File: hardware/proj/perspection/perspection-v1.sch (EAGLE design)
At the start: 233 parts, among them J1 MICRO-USB-10118192-0001LF, J2 1X6-PTSA_1.5/6-3.5-Z, J3 1X2-PTSA_1.5/2-3.5-Z, J4 1X2-JST-PH-SMD, J5 1X2-0428202213, J6 JTAG-ARM_TC-10, J7 JTAG-ARM_TC-10, J8 1X3-0.1IN_THRUHOLE, Q1 NMOS-CSD18533Q5A, Q10 NMOS-CSD18533Q5A, Q11 IRFML8244TRPBF, Q2 NMOS-CSD18533Q5A, Q3 NMOS-CSD18533Q5A, Q4 NMOS-CSD18533Q5A, Q5 NMOS-CSD18533Q5A, Q6 NMOS-CSD18533Q5A, Q7 NMOS-CSD18533Q5A, Q8 BSS138L, Q9 BSS138L, U1 ATUM, U10 DRV8301DCAR, U11 OPA2374AIDCNR, U12 OPA170AIDBVR, U13 BNO055, U2 FT232RQ, U3 TPS79933DDCR, U4 MCP73831T-2ACI/OT, U5 TMS320F28069MPZT, U6 DRV8801PWPR, U7 DRV8801PWPR, U8 DRV8801PWPR, U9 DRV8801PWPR, Y1 32.768kHz

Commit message: holy fucking shit 81 airwires to go
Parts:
- added J9: 1X2-PTSA_1.5/2-3.5-Z, perspection:1X2-PTSA_1.5/2-3.5-Z
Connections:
- net N$6 renamed D_P
- net N$7 renamed D_N
- new net N$16: C69.1, U5.1.VDD4
- new net N$17: C68.1, U5.1.VDD3
- new net N$21: C66.1, U5.1.VDD1
- new net N$6: C71.1, U5.1.VDD6
- new net N$7: C70.1, U5.1.VDD5
- net +12V: now also J9.1
- net +12V_GND: now also J9.2
- net N$58: now also U5.1.VDD2; no longer C66.1, C68.1, C69.1, C70.1, C71.1, U5.1.VDD
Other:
- moved on the sheet: C66, C67, C68, C69, C70, C71, C72, C73, C74, C75, C76, C77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

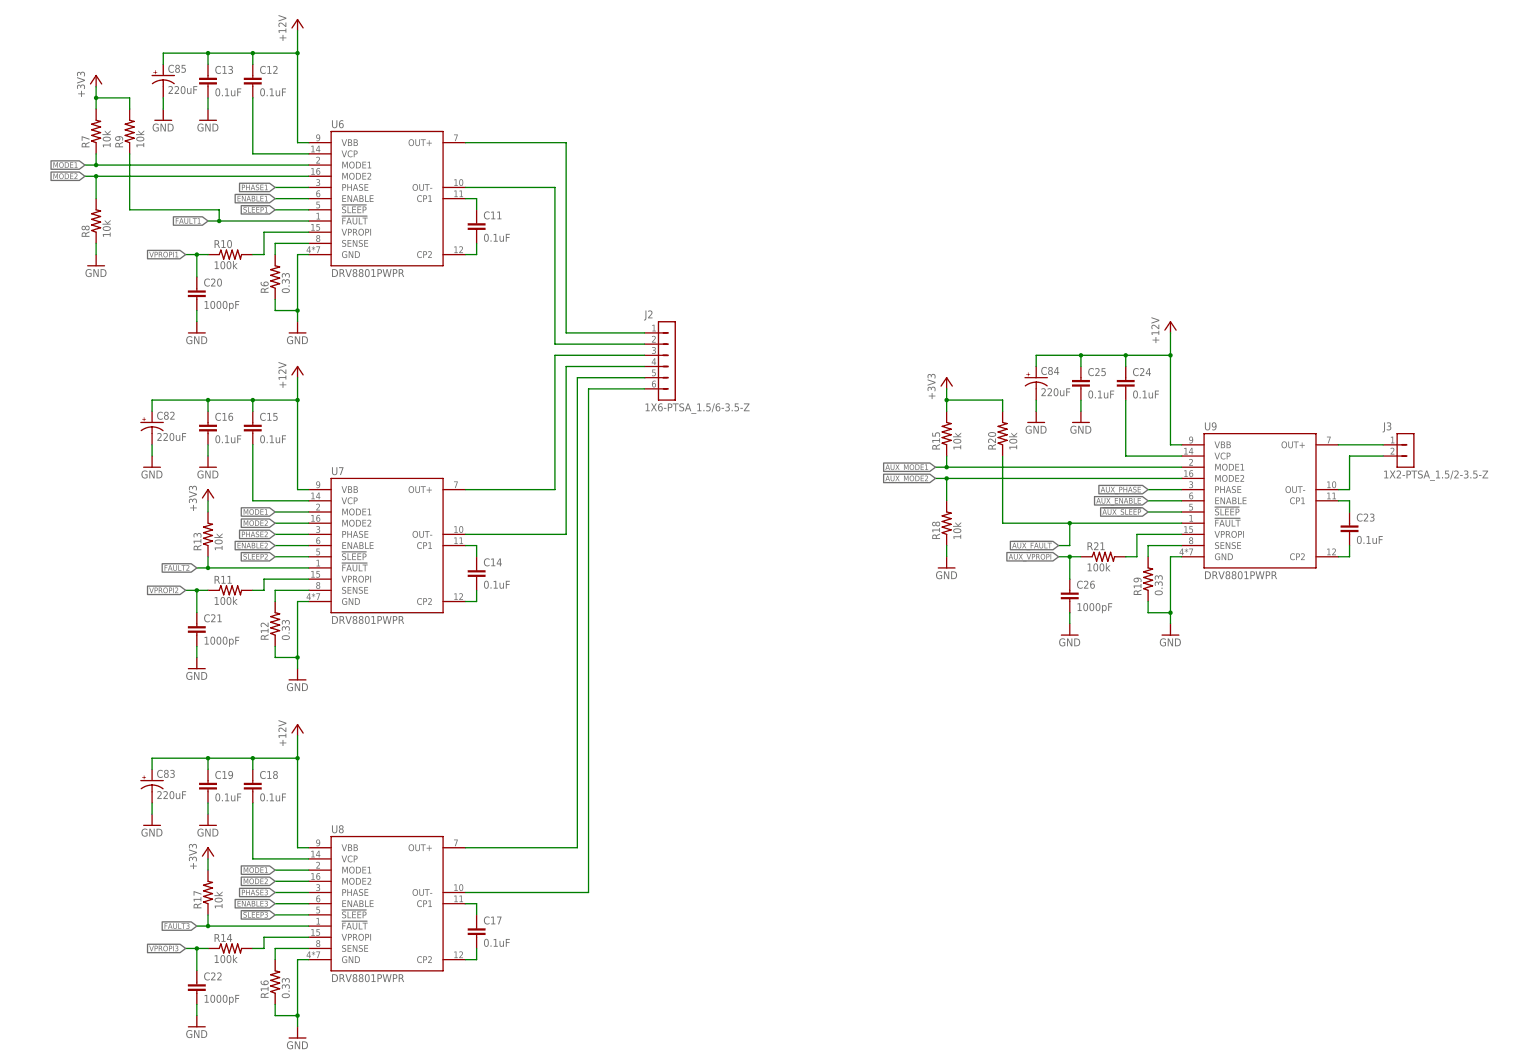
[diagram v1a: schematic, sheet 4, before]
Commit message: 26 airwires!
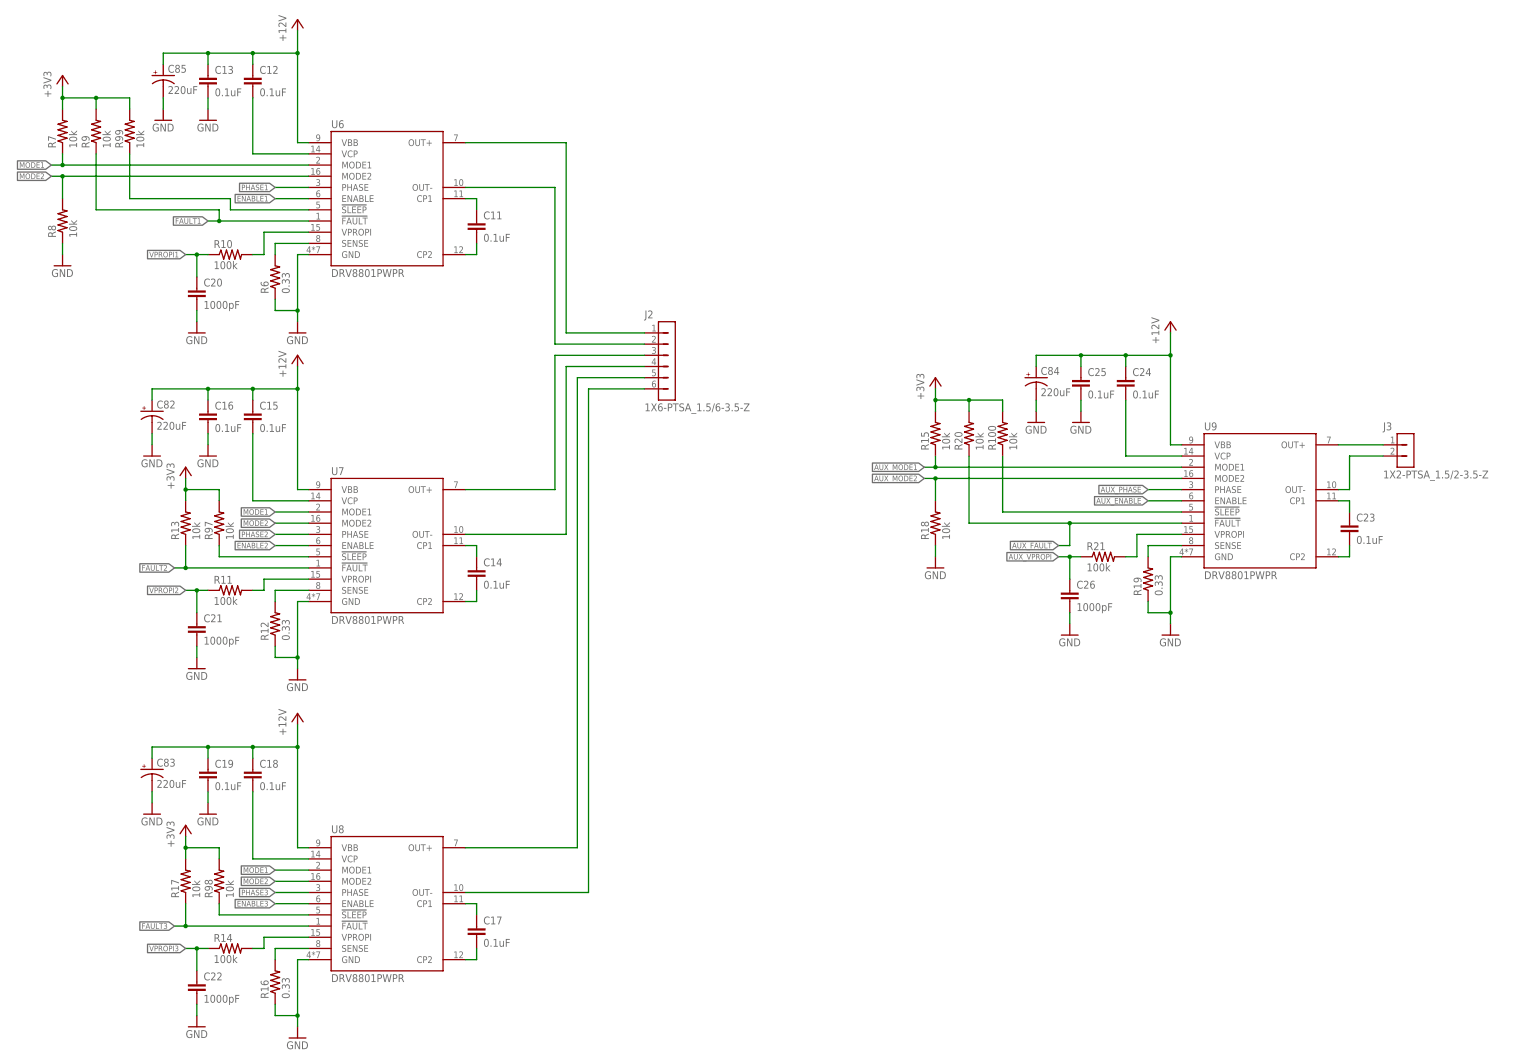
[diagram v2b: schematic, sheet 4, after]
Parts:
- added R100, R97, R98, R99: 10k, perspection:R0402
- added R101, R102, R103, R104, R105, R106, R107, R108, R93, R94, R95, R96: 0, perspection:R0402
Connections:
- net N$16 renamed VDD4
- net N$17 renamed VDD3
- net N$21 renamed VDD1
- net N$58 renamed VDD2
- net N$6 renamed VDD6
- net N$7 renamed VDD5
- removed net ATUM_B3: U1.B3
- removed net ATUM_B4: U1.B4
- new net ATUM_ENCODER_A: R107.1
- new net ATUM_ENCODER_B: R108.1
- new net N$25: R93.1, U5.1.ADC_INB2/COMP1B/AIO10
- new net N$26: R94.1, U5.1.ADC_INB1
- new net N$27: R95.1, U5.1.ADC_INB0
- new net N$31: R96.1, U5.1.ADC_INA6/COMP3A/AIO6
- new net N$32: R102.2, U5.2.GPIO3/EPWM2B/SPISOMIA/COMP2OUT
- new net N$43: R103.2, U5.2.GPIO2/EPWM2A
- new net N$44: R104.2, U5.2.GPIO1/EPWM1B/COMP1OUT
- new net N$46: R101.2, U5.2.GPIO0/EPWM1A
- new net N$47: R105.2, U1.B4
- new net N$48: R106.2, U1.B3
- net !AUX_SLEEP: now also R100.1
- net !SLEEP1: now also R99.1
- net !SLEEP2: now also R97.1
- net !SLEEP3: now also R98.1
- net +3V3: now also R100.2, R97.2, R98.2, R99.2
- net ATUM_C0: now also R108.2
- net ATUM_C1: now also R107.2
- net AUX_ENABLE: now also R101.1, R105.1
- net AUX_PHASE: now also R106.1
- net AUX_VPROPI: now also R96.2
- net ENABLE1: now also R104.1
- net ENABLE2: now also R103.1
- net ENABLE3: now also R102.1
- net VPROPI1: now also R95.2
- net VPROPI2: now also R94.2
- net VPROPI3: now also R93.2
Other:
- moved on the sheet: C15, C16, C18, C19, C82, C83, R13, R15, R17, R18, R20, R40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

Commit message: JASON TAKE THE WHEEL
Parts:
- added C95: 4.7uF, perspection:C0603
- added J10: 1X5, perspection:1X5
- added R109, R111, R113: 23.2k, perspection:R0402
- added R110, R112, R114: 45.2k, perspection:R0402
- added R115, R116, R117, R118: 0, perspection:R0402
- added R119, R120, R121, R122: (no value), perspection:R0402
- added U14: TPS81256, perspection:TPS81256
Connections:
- net N$91 renamed PICCOLO_TMS
- net N$92 renamed PICCOLO_TCK
- net N$93 renamed PICCOLO_TDI
- net N$95 renamed !PICCOLO_TRST
- removed net ATUM_C2: U1.C2
- removed net ATUM_ENCODER_A: R107.1
- removed net ATUM_ENCODER_B: R108.1
- removed net N$94: J7.TDO, U5.1.TDO/GPIO37
- new net !SPI_CS: R117.2, U1.C2
- new net ENC_PWR: C95.1, J10.2, U14.VOUT
- new net EQEP1A: R107.1, R111.1, R112.2, U5.2.GPIO20/EQEP1A/MDXA/COMP1OUT
- new net EQEP1B: R108.1, R109.1, R110.2, U5.2.GPIO21/EQEP1B/MDRA/COMP2OUT
- new net EQEP1I: R113.1, R114.2, U5.2.GPIO23/EQEP1I/MFSXA/SCIRXDB
- new net GPIO_34: R121.1, R122.2, U5.2.GPIO34/COMP2OUT/COMP3OUT
- new net N$16: J10.3, R111.2
- new net N$17: J10.4, R113.2
- new net N$6: J10.1, R109.2
- new net PICCOLO_TDO: J7.TDO, R119.1, R120.2, U5.1.TDO/GPIO37
- new net _!SPI_CS: R117.1, U5.2.GPIO57/!SPISTEA!/EQEP2S/HRCAP4
- new net _SPI_MISO: R116.1, U5.2.GPIO55/SPISOMIA/EQEP2B/HRCAP2
- new net _SPI_MOSI: R115.1, U5.2.GPIO54/SPISIMOA/EQEP2A/HRCAP1
- new net _SPI_SCK: R118.1, U5.2.GPIO56/SPICLKA/EQEP2I/HRCAP3
- net +3V3: now also R119.2, R121.2, U14.EN, U14.VIN
- net GND: now also C95.2, J10.5, R110.1, R112.1, R114.1, R120.1, R122.1, U14.GND
- net SPI_MISO: now also R116.2
- net SPI_MOSI: now also R115.2
- net SPI_SCK: now also R118.2
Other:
- moved on the sheet: J7, R107, R108, R42, R59, R60

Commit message: blarg
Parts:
- added C96: 0.1uF, perspection:C0402
- added R123: 0, perspection:R0402
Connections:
- removed net ATUM_ADC3: U1.ADC3
- new net N$7: C96.1, R123.1, U1.ADC3
- net AUX_VPROPI: now also R123.2
- net GND: now also C96.2
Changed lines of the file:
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@@
 <setting verticaltext="up"/>
 </settings>
-<grid distance="0.1" unitdist="inch" unit="inch" style="lines" multiple="1" display="yes" altdistance="0.01" altunitdist="inch" altunit="inch"/>
+<grid distance="0.1" unitdist="inch" unit="inch" style="lines" multiple="1" display="no" altdistance="0.01" altunitdist="inch" altunit="inch"/>
 <layers>
 <layer number="1" name="Top" color="4" fill="1" visible="no" active="no"/>
@@
 <part name="R122" library="perspection" deviceset="R" device="0402"/>
 <part name="GND88" library="perspection" deviceset="GND" device=""/>
+<part name="R123" library="perspection" deviceset="R" device="0402" value="0"/>
+<part name="C96" library="perspection" deviceset="C" device="0402" value="0.1uF"/>
+<part name="GND89" library="perspection" deviceset="GND" device=""/>
 </parts>
 <sheets>
@@
 <instance part="R107" gate="G$1" x="231.14" y="147.32"/>
 <instance part="R108" gate="G$1" x="231.14" y="139.7"/>
+<instance part="R123" gate="G$1" x="284.48" y="187.96"/>
+<instance part="C96" gate="G$1" x="276.86" y="182.88"/>
+<instance part="GND89" gate="1" x="276.86" y="172.72"/>
 </instances>
 <busses>
@@
 <pinref part="GND81" gate="1" pin="GND"/>
 </segment>
+<segment>
+<pinref part="C96" gate="G$1" pin="2"/>
+<pinref part="GND89" gate="1" pin="GND"/>
+<wire x1="276.86" y1="175.26" x2="276.86" y2="177.8" width="0.1524" layer="91"/>
+</segment>
 </net>
 <net name="BOOTLOADER_RX" class="0">
@@
 <pinref part="U1" gate="G$1" pin="BTLDR_CTRL"/>
 <wire x1="269.24" y1="187.96" x2="271.78" y2="187.96" width="0.1524" layer="91"/>
-<label x="271.78" y="187.96" size="1.27" layer="95" xref="yes"/>
+<wire x1="271.78" y1="187.96" x2="271.78" y2="167.64" width="0.1524" layer="91"/>
+<wire x1="271.78" y1="167.64" x2="274.32" y2="167.64" width="0.1524" layer="91"/>
+<label x="274.32" y="167.64" size="1.27" layer="95" xref="yes"/>
 </segment>
 <segment>
@@
 <wire x1="246.38" y1="170.18" x2="246.38" y2="139.7" width="0.1524" layer="91"/>
 <wire x1="246.38" y1="139.7" x2="236.22" y2="139.7" width="0.1524" layer="91"/>
-</segment>
-</net>
-<net name="ATUM_ADC3" class="0">
-<segment>
-<pinref part="U1" gate="G$1" pin="ADC3"/>
-<wire x1="269.24" y1="190.5" x2="271.78" y2="190.5" width="0.1524" layer="91"/>
-<label x="271.78" y="190.5" size="1.27" layer="95" xref="yes"/>
 </segment>
 </net>
@@
 </segment>
 </net>
+<net name="N$7" class="0">
+<segment>
+<pinref part="U1" gate="G$1" pin="ADC3"/>
+<pinref part="R123" gate="G$1" pin="1"/>
+<wire x1="279.4" y1="187.96" x2="276.86" y2="187.96" width="0.1524" layer="91"/>
+<wire x1="276.86" y1="187.96" x2="274.32" y2="187.96" width="0.1524" layer="91"/>
+<wire x1="274.32" y1="187.96" x2="274.32" y2="190.5" width="0.1524" layer="91"/>
+<wire x1="274.32" y1="190.5" x2="269.24" y2="190.5" width="0.1524" layer="91"/>
+<pinref part="C96" gate="G$1" pin="1"/>
+<wire x1="276.86" y1="185.42" x2="276.86" y2="187.96" width="0.1524" layer="91"/>
+<junction x="276.86" y="187.96"/>
+</segment>
+</net>
+<net name="AUX_VPROPI" class="0">
+<segment>
+<pinref part="R123" gate="G$1" pin="2"/>
+<label x="292.1" y="187.96" size="1.27" layer="95" xref="yes"/>
+<wire x1="289.56" y1="187.96" x2="292.1" y2="187.96" width="0.1524" layer="91"/>
+</segment>
+</net>

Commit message: pretty much done, need to compile BOM
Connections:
- removed net _!OCTW: R42.1, U5.2.GPIO58/MCLKRA/SCI_TXDB/EPWM7A
- removed net _DRV_SDI: R57.2, U5.2.GPIO24/ECAP1/EQEP2A/SPISIMOB
- new net N$21: R57.2, U5.2.GPIO28/SCI_RXDA/SDAA/!TZ2
- new net N$49: R42.1, U5.2.GPIO29/SCI_TXDA/SCLA/!TZ3
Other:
- moved on the sheet: R42, R56, R57
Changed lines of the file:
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@@
 <instance part="R40" gate="G$1" x="78.74" y="45.72"/>
 <instance part="R41" gate="G$1" x="78.74" y="53.34"/>
-<instance part="R42" gate="G$1" x="254" y="17.78"/>
+<instance part="R42" gate="G$1" x="243.84" y="76.2"/>
 <instance part="R43" gate="G$1" x="314.96" y="167.64"/>
 <instance part="R44" gate="G$1" x="314.96" y="157.48"/>
@@
 <instance part="R54" gate="G$1" x="78.74" y="63.5"/>
 <instance part="R55" gate="G$1" x="71.12" y="58.42"/>
-<instance part="R56" gate="G$1" x="246.38" y="86.36"/>
-<instance part="R57" gate="G$1" x="96.52" y="30.48"/>
+<instance part="R56" gate="G$1" x="243.84" y="86.36"/>
+<instance part="R57" gate="G$1" x="248.92" y="81.28" rot="R180"/>
 <instance part="R58" gate="G$1" x="96.52" y="22.86"/>
 <instance part="R59" gate="G$1" x="254" y="48.26"/>
@@
 </segment>
 </net>
-<net name="_!OCTW" class="0">
-<segment>
-<pinref part="U5" gate=".2" pin="GPIO58/MCLKRA/SCI_TXDB/EPWM7A"/>
-<pinref part="R42" gate="G$1" pin="1"/>
-<wire x1="248.92" y1="17.78" x2="236.22" y2="17.78" width="0.1524" layer="91"/>
-<wire x1="236.22" y1="17.78" x2="236.22" y2="25.4" width="0.1524" layer="91"/>
-<wire x1="236.22" y1="25.4" x2="226.06" y2="25.4" width="0.1524" layer="91"/>
-</segment>
-</net>
 <net name="_DC_V_FB" class="0">
 <segment>
@@
 <pinref part="U5" gate=".2" pin="GPIO27/HRCAP2/EQEP2S/!SPISTEB!/USB0DM"/>
 <pinref part="R56" gate="G$1" pin="1"/>
-<wire x1="241.3" y1="86.36" x2="226.06" y2="86.36" width="0.1524" layer="91"/>
-</segment>
-</net>
-<net name="_DRV_SDI" class="0">
-<segment>
-<pinref part="U5" gate=".2" pin="GPIO24/ECAP1/EQEP2A/SPISIMOB"/>
-<pinref part="R57" gate="G$1" pin="2"/>
-<wire x1="101.6" y1="30.48" x2="104.14" y2="30.48" width="0.1524" layer="91"/>
-<wire x1="104.14" y1="30.48" x2="104.14" y2="27.94" width="0.1524" layer="91"/>
-<wire x1="104.14" y1="27.94" x2="119.38" y2="27.94" width="0.1524" layer="91"/>
+<wire x1="238.76" y1="86.36" x2="226.06" y2="86.36" width="0.1524" layer="91"/>
 </segment>
 </net>
@@
 <segment>
 <pinref part="R57" gate="G$1" pin="1"/>
-<wire x1="91.44" y1="30.48" x2="78.74" y2="30.48" width="0.1524" layer="91"/>
-<label x="78.74" y="30.48" size="1.27" layer="95" rot="R180" xref="yes"/>
+<wire x1="254" y1="81.28" x2="261.62" y2="81.28" width="0.1524" layer="91"/>
+<label x="261.62" y="81.28" size="1.27" layer="95" xref="yes"/>
 </segment>
 </net>
@@
 <segment>
 <pinref part="R42" gate="G$1" pin="2"/>
-<wire x1="259.08" y1="17.78" x2="261.62" y2="17.78" width="0.1524" layer="91"/>
-<label x="261.62" y="17.78" size="1.27" layer="95" xref="yes"/>
+<wire x1="248.92" y1="76.2" x2="261.62" y2="76.2" width="0.1524" layer="91"/>
+<label x="261.62" y="76.2" size="1.27" layer="95" xref="yes"/>
 </segment>
 </net>
@@
 <segment>
 <pinref part="R56" gate="G$1" pin="2"/>
-<wire x1="251.46" y1="86.36" x2="256.54" y2="86.36" width="0.1524" layer="91"/>
-<label x="256.54" y="86.36" size="1.27" layer="95" xref="yes"/>
+<wire x1="248.92" y1="86.36" x2="261.62" y2="86.36" width="0.1524" layer="91"/>
+<label x="261.62" y="86.36" size="1.27" layer="95" xref="yes"/>
 </segment>
 </net>
@@
 </segment>
 </net>
+<net name="N$21" class="0">
+<segment>
+<pinref part="U5" gate=".2" pin="GPIO28/SCI_RXDA/SDAA/!TZ2"/>
+<wire x1="226.06" y1="83.82" x2="236.22" y2="83.82" width="0.1524" layer="91"/>
+<wire x1="236.22" y1="83.82" x2="236.22" y2="81.28" width="0.1524" layer="91"/>
+<wire x1="236.22" y1="81.28" x2="243.84" y2="81.28" width="0.1524" layer="91"/>
+<pinref part="R57" gate="G$1" pin="2"/>
+</segment>
+</net>
+<net name="N$49" class="0">
+<segment>
+<pinref part="U5" gate=".2" pin="GPIO29/SCI_TXDA/SCLA/!TZ3"/>
+<wire x1="226.06" y1="81.28" x2="233.68" y2="81.28" width="0.1524" layer="91"/>
+<wire x1="233.68" y1="81.28" x2="233.68" y2="76.2" width="0.1524" layer="91"/>
+<wire x1="233.68" y1="76.2" x2="238.76" y2="76.2" width="0.1524" layer="91"/>
+<pinref part="R42" gate="G$1" pin="1"/>
+</segment>
+</net>
